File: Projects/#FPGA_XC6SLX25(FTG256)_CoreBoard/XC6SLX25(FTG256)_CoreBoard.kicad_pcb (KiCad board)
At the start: 2 copper layers, 69.6 x 30 mm, 2 parts, among them J1 MTA18ASF2G72HZ-2G3A1, U1 XC6SLX25-FTG256

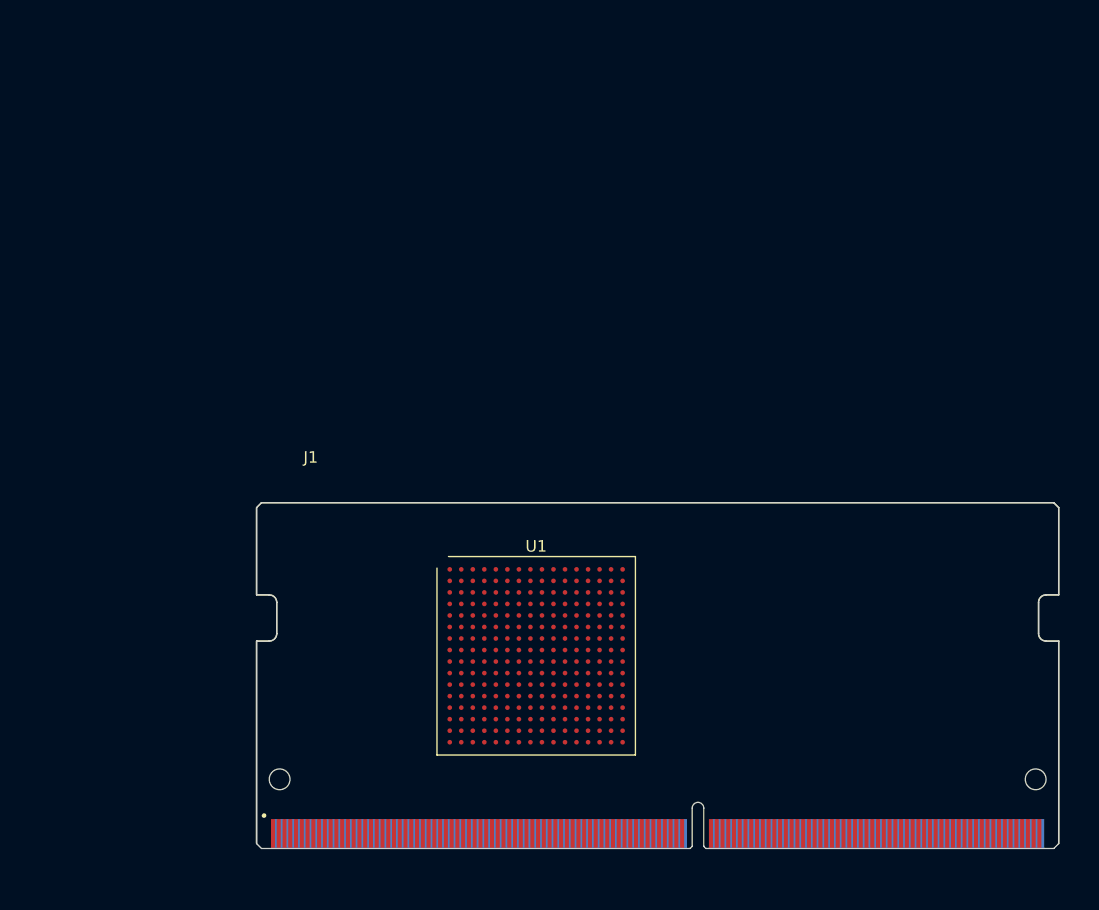
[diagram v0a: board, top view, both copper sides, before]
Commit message: Update XC6SLX25(FTG256)_CoreBoard
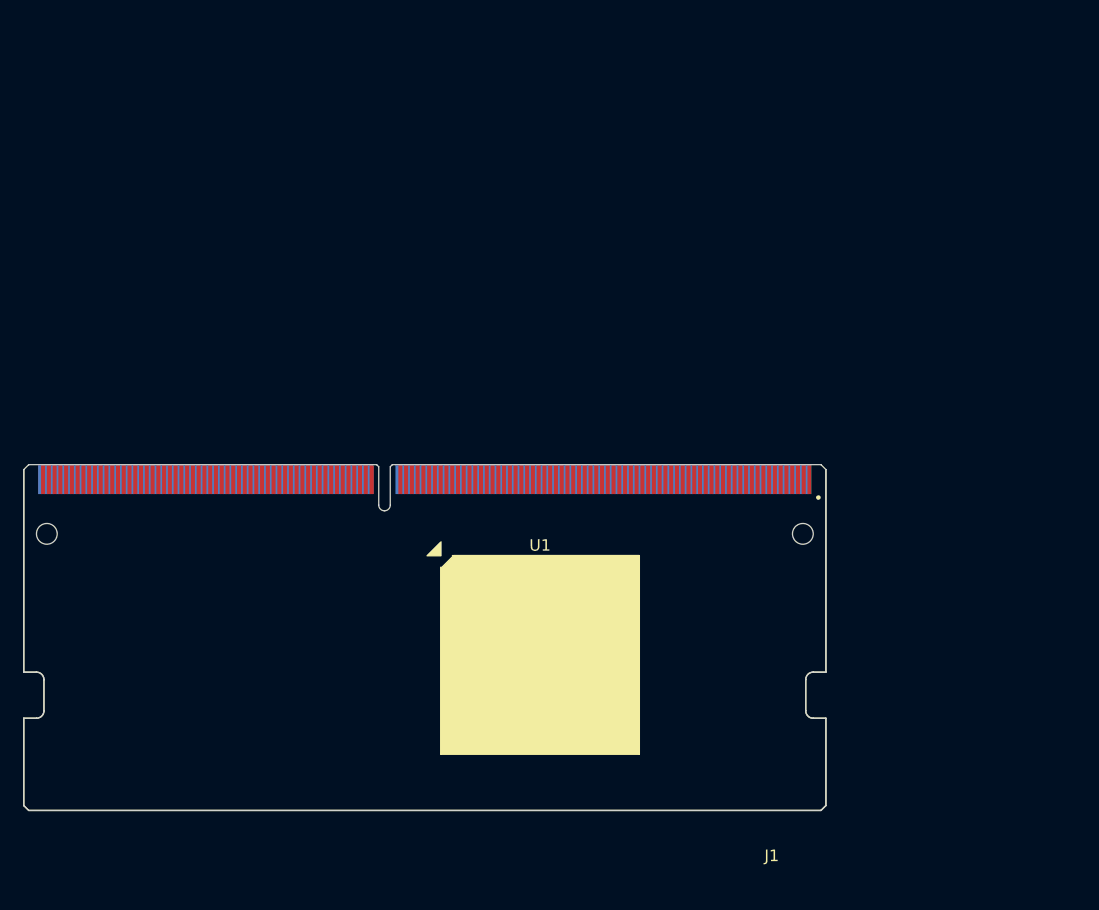
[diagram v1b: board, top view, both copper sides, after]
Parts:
- moved J1 20.5 mm to (122.0, 80.5), turned to 180 degrees
- moved U1 0.35 mm to (132.0, 82.0)
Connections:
- U1 pad A1: unconnected-(U1-PadA1) -> GND
- U1 pad A16: unconnected-(U1-PadA16) -> GND
- U1 pad B11: unconnected-(U1-PadB11) -> GND
- U1 pad B13: unconnected-(U1-PadB13) -> +3V3
- U1 pad B4: unconnected-(U1-PadB4) -> +3V3
- U1 pad B7: unconnected-(U1-PadB7) -> GND
- U1 pad B9: unconnected-(U1-PadB9) -> +3V3
- U1 pad D10: unconnected-(U1-PadD10) -> +3V3
- U1 pad D13: unconnected-(U1-PadD13) -> GND
- U1 pad D15: unconnected-(U1-PadD15) -> +2V5
- U1 pad D2: unconnected-(U1-PadD2) -> +1V5
- U1 pad D4: unconnected-(U1-PadD4) -> GND
- U1 pad D7: unconnected-(U1-PadD7) -> +3V3
- U1 pad E5: unconnected-(U1-PadE5) -> +3V3
- U1 pad E9: unconnected-(U1-PadE9) -> GND
- U1 pad F11: unconnected-(U1-PadF11) -> +3V3
- U1 pad F8: unconnected-(U1-PadF8) -> +3V3
- U1 pad G10: unconnected-(U1-PadG10) -> +3V3
- U1 pad G13: unconnected-(U1-PadG13) -> +2V5
- U1 pad G15: unconnected-(U1-PadG15) -> GND
- U1 pad G2: unconnected-(U1-PadG2) -> GND
- U1 pad G4: unconnected-(U1-PadG4) -> +1V5
- U1 pad G7: unconnected-(U1-PadG7) -> +1V2
- U1 pad G8: unconnected-(U1-PadG8) -> GND
- U1 pad G9: unconnected-(U1-PadG9) -> +1V2
- U1 pad H10: unconnected-(U1-PadH10) -> +1V2
- U1 pad H12: unconnected-(U1-PadH12) -> GND
- U1 pad H6: unconnected-(U1-PadH6) -> +3V3
- U1 pad H7: unconnected-(U1-PadH7) -> GND
- U1 pad H8: unconnected-(U1-PadH8) -> +1V2
- U1 pad H9: unconnected-(U1-PadH9) -> GND
- U1 pad J10: unconnected-(U1-PadJ10) -> +3V3
- U1 pad J15: unconnected-(U1-PadJ15) -> +2V5
- U1 pad J2: unconnected-(U1-PadJ2) -> +1V5
- U1 pad J5: unconnected-(U1-PadJ5) -> GND
- U1 pad J7: unconnected-(U1-PadJ7) -> +1V2
- U1 pad J8: unconnected-(U1-PadJ8) -> GND
- U1 pad J9: unconnected-(U1-PadJ9) -> +1V2
- U1 pad K10: unconnected-(U1-PadK10) -> +1V2
- U1 pad K13: unconnected-(U1-PadK13) -> +2V5
- U1 pad K4: unconnected-(U1-PadK4) -> +1V5
- U1 pad K7: unconnected-(U1-PadK7) -> GND
- U1 pad K8: unconnected-(U1-PadK8) -> +1V2
- U1 pad K9: unconnected-(U1-PadK9) -> GND
- U1 pad L15: unconnected-(U1-PadL15) -> GND
- U1 pad L2: unconnected-(U1-PadL2) -> GND
- U1 pad L6: unconnected-(U1-PadL6) -> +3V3
- U1 pad L9: unconnected-(U1-PadL9) -> +3V3
- U1 pad M8: unconnected-(U1-PadM8) -> GND
- U1 pad N10: unconnected-(U1-PadN10) -> +3V3
- U1 pad N13: unconnected-(U1-PadN13) -> GND
- U1 pad N15: unconnected-(U1-PadN15) -> +2V5
- U1 pad N2: unconnected-(U1-PadN2) -> +1V5
- U1 pad N7: unconnected-(U1-PadN7) -> +3V3
- U1 pad P3: unconnected-(U1-PadP3) -> GND
- U1 pad R10: unconnected-(U1-PadR10) -> GND
- U1 pad R13: unconnected-(U1-PadR13) -> +2V5
- U1 pad R4: unconnected-(U1-PadR4) -> +3V3
- U1 pad R6: unconnected-(U1-PadR6) -> GND
- U1 pad R8: unconnected-(U1-PadR8) -> +3V3
- U1 pad T1: unconnected-(U1-PadT1) -> GND
- U1 pad T16: unconnected-(U1-PadT16) -> GND
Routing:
- net GND: track 0.00 -> 17.0 mm, vias 0 -> 22
- net +3V3: track 0.00 -> 12.7 mm, vias 0 -> 17
- net +1V2: track 0.00 -> 9.90 mm, vias 0 -> 6
- net +2V5: track 0.00 -> 4.24 mm, vias 0 -> 6
- net +1V5: track 0.00 -> 3.54 mm, vias 0 -> 5
- net unconnected-(U1-PadR12): track 0.00 -> 0.71 mm, vias 0 -> 1
- net unconnected-(U1-PadP4): track 0.00 -> 0.71 mm, vias 0 -> 1
- net unconnected-(U1-PadN6): track 0.00 -> 0.71 mm, vias 0 -> 1
- net unconnected-(U1-PadN14): track 0.00 -> 0.71 mm, vias 0 -> 1
- net unconnected-(U1-PadN11): track 0.00 -> 0.71 mm, vias 0 -> 1
- net unconnected-(U1-PadM7): track 0.00 -> 0.71 mm, vias 0 -> 1
- net unconnected-(U1-PadM2): track 0.00 -> 0.71 mm, vias 0 -> 1
- net unconnected-(U1-PadL8): track 0.00 -> 0.71 mm, vias 0 -> 1
- net unconnected-(U1-PadL4): track 0.00 -> 0.71 mm, vias 0 -> 1
- net unconnected-(U1-PadL13): track 0.00 -> 0.71 mm, vias 0 -> 1
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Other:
- outline, holes or cut-outs redrawn
- copper layers 2 -> 6

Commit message: Update XC6SLX25(FTG256)_CoreBoard
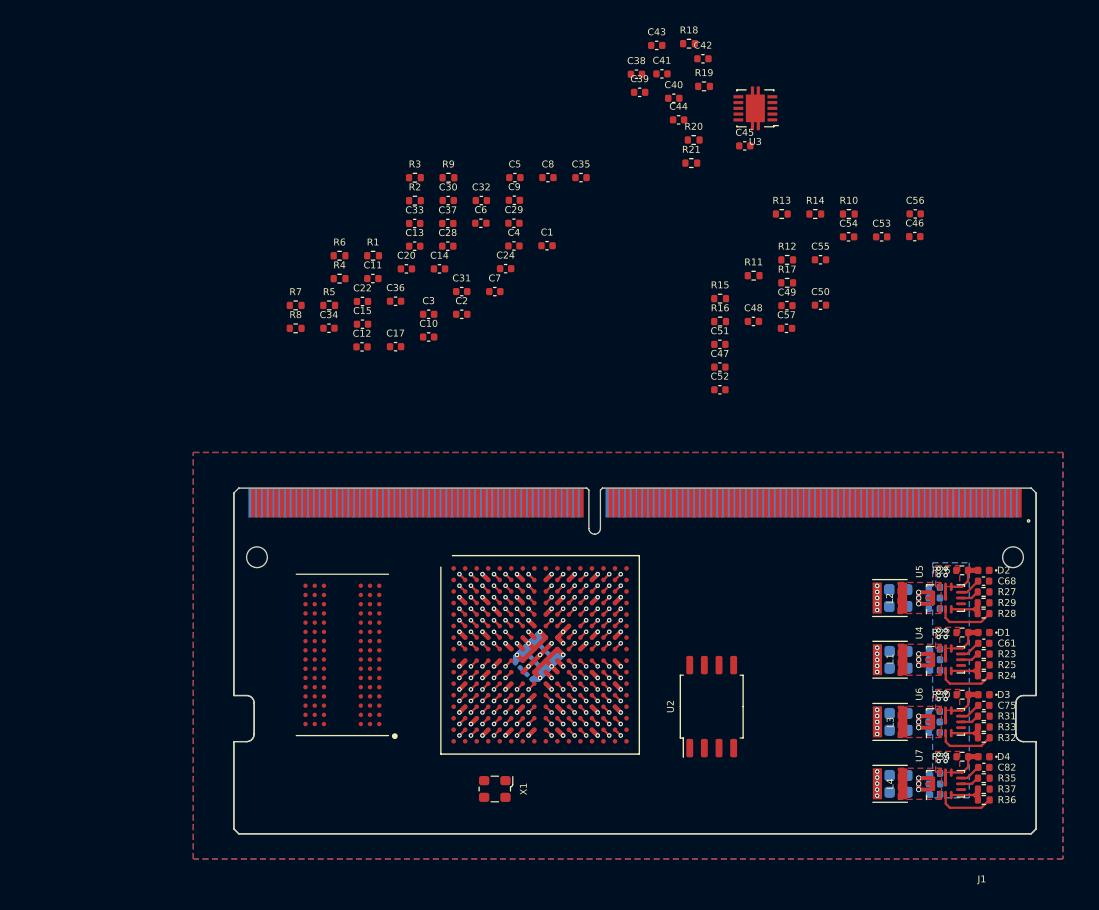
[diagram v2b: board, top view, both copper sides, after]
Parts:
- added C1: 0.1uF, Capacitor_SMD:C_0402_1005Metric, F.Cu at (132.6, 46.5)
- added C10: 10nF, Capacitor_SMD:C_0402_1005Metric, F.Cu at (122.3, 54.4)
- added C11: 0.1uF, Capacitor_SMD:C_0402_1005Metric, F.Cu at (117.5, 49.4)
- added C12: 0.1uF, Capacitor_SMD:C_0402_1005Metric, F.Cu at (116.5, 55.3)
- added C13: 10nF, Capacitor_SMD:C_0402_1005Metric, F.Cu at (121.1, 46.5)
- added C14: 0.1uF, Capacitor_SMD:C_0402_1005Metric, F.Cu at (123.3, 48.5)
- added C15: 10nF, Capacitor_SMD:C_0402_1005Metric, F.Cu at (116.6, 53.3)
- added C16: 0.1uF, Capacitor_SMD:C_0201_0603Metric, B.Cu at (131.0, 82.0)
- added C17: 0.1uF, Capacitor_SMD:C_0402_1005Metric, F.Cu at (119.5, 55.3)
- added C18: 10nF, Capacitor_SMD:C_0201_0603Metric, B.Cu at (130.1, 82.9)
- added C19: 0.1uF, Capacitor_SMD:C_0201_0603Metric, B.Cu at (132.9, 82.1)
- added C2: 10nF, Capacitor_SMD:C_0402_1005Metric, F.Cu at (125.2, 52.5)
- added C20: 10nF, Capacitor_SMD:C_0402_1005Metric, F.Cu at (120.4, 48.5)
- added C21: 10nF, Capacitor_SMD:C_0201_0603Metric, B.Cu at (131.9, 81.1)
- added C22: 0.1uF, Capacitor_SMD:C_0402_1005Metric, F.Cu at (116.6, 51.3)
- added C23: 0.1uF, Capacitor_SMD:C_0201_0603Metric, B.Cu at (132.0, 83.0)
- added C24: 10nF, Capacitor_SMD:C_0402_1005Metric, F.Cu at (129.0, 48.5)
- added C25: 10nF, Capacitor_SMD:C_0201_0603Metric, B.Cu at (131.1, 83.9)
- added C28: 0.1uF, Capacitor_SMD:C_0402_1005Metric, F.Cu at (124.0, 46.5)
- added C29: 10nF, Capacitor_SMD:C_0402_1005Metric, F.Cu at (129.7, 44.5)
- added C3: 0.1uF, Capacitor_SMD:C_0402_1005Metric, F.Cu at (122.3, 52.5)
- added C30: 0.1uF, Capacitor_SMD:C_0402_1005Metric, F.Cu at (124.0, 42.6)
- added C31: 10nF, Capacitor_SMD:C_0402_1005Metric, F.Cu at (125.2, 50.5)
- added C32: 0.1uF, Capacitor_SMD:C_0402_1005Metric, F.Cu at (126.9, 42.6)
- added C33: 10nF, Capacitor_SMD:C_0402_1005Metric, F.Cu at (121.1, 44.6)
- added C34: 0.1uF, Capacitor_SMD:C_0402_1005Metric, F.Cu at (113.7, 53.7)
- added C35: 10nF, Capacitor_SMD:C_0402_1005Metric, F.Cu at (135.6, 40.6)
- added C36: 0.1uF, Capacitor_SMD:C_0402_1005Metric, F.Cu at (119.5, 51.3)
- added C37: 10nF, Capacitor_SMD:C_0402_1005Metric, F.Cu at (124.0, 44.6)
- added C38: 10uF, Capacitor_SMD:C_0402_1005Metric, F.Cu at (140.4, 31.6)
- added C39: 10uF, Capacitor_SMD:C_0402_1005Metric, F.Cu at (140.6, 33.2)
- added C4: 0.1uF, Capacitor_SMD:C_0402_1005Metric, F.Cu at (129.7, 46.5)
- added C40: 10uF, Capacitor_SMD:C_0402_1005Metric, F.Cu at (143.6, 33.7)
- added C41: 10uF, Capacitor_SMD:C_0402_1005Metric, F.Cu at (142.6, 31.6)
- added C42: 1nF, Capacitor_SMD:C_0402_1005Metric, F.Cu at (146.1, 30.3)
- added C43: 10uF, Capacitor_SMD:C_0402_1005Metric, F.Cu at (142.1, 29.1)
- added C44: 0.1uF, Capacitor_SMD:C_0402_1005Metric, F.Cu at (144.0, 35.6)
- added C45: 4.7uF, Capacitor_SMD:C_0402_1005Metric, F.Cu at (149.8, 37.8)
- added C46: 0.1uF, Capacitor_SMD:C_0402_1005Metric, F.Cu at (164.5, 45.7)
- added C47: 0.1uF, Capacitor_SMD:C_0402_1005Metric, F.Cu at (147.6, 57.0)
- added C48: 0.1uF, Capacitor_SMD:C_0402_1005Metric, F.Cu at (150.5, 53.1)
- added C49: 0.1uF, Capacitor_SMD:C_0402_1005Metric, F.Cu at (153.4, 51.7)
- added C5: 10nF, Capacitor_SMD:C_0402_1005Metric, F.Cu at (129.8, 40.6)
- added C50: 0.1uF, Capacitor_SMD:C_0402_1005Metric, F.Cu at (156.3, 51.7)
- added C51: 0.1uF, Capacitor_SMD:C_0402_1005Metric, F.Cu at (147.6, 55.1)
- added C52: 0.1uF, Capacitor_SMD:C_0402_1005Metric, F.Cu at (147.6, 59.0)
- added C53: 0.1uF, Capacitor_SMD:C_0402_1005Metric, F.Cu at (161.6, 45.7)
- added C54: 0.1uF, Capacitor_SMD:C_0402_1005Metric, F.Cu at (158.8, 45.7)
- added C55: 0.1uF, Capacitor_SMD:C_0402_1005Metric, F.Cu at (156.3, 47.7)
- added C56: 0.1uF, Capacitor_SMD:C_0402_1005Metric, F.Cu at (164.6, 43.7)
- added C57: 0.1uF, Capacitor_SMD:C_0402_1005Metric, F.Cu at (153.4, 53.7)
- added C58: 10uF, Capacitor_SMD:C_0402_1005Metric, B.Cu at (166.2, 81.5)
- added C59: 10uF, Capacitor_SMD:C_0402_1005Metric, B.Cu at (166.2, 83.3)
- added C6: 10nF, Capacitor_SMD:C_0402_1005Metric, F.Cu at (126.9, 44.5)
- added C60: 0.1uF, Capacitor_SMD:C_0402_1005Metric, B.Cu at (166.2, 82.4)
- added C61: 1uF, Capacitor_SMD:C_0402_1005Metric, F.Cu at (170.5, 81.0)
- added C63: 22uF, Capacitor_SMD:C_0603_1608Metric, B.Cu at (163.1, 83.2)
- added C64: 22uF, Capacitor_SMD:C_0603_1608Metric, B.Cu at (163.1, 81.7)
- added C65: 10uF, Capacitor_SMD:C_0402_1005Metric, B.Cu at (166.2, 76.1)
- added C66: 10uF, Capacitor_SMD:C_0402_1005Metric, B.Cu at (166.2, 77.1)
- added C67: 0.1uF, Capacitor_SMD:C_0402_1005Metric, B.Cu at (166.2, 78.0)
- added C68: 1uF, Capacitor_SMD:C_0402_1005Metric, F.Cu at (170.5, 75.6)
- added C7: 0.1uF, Capacitor_SMD:C_0402_1005Metric, F.Cu at (128.1, 50.5)
- added C70: 22uF, Capacitor_SMD:C_0603_1608Metric, B.Cu at (163.1, 77.8)
- added C71: 22uF, Capacitor_SMD:C_0603_1608Metric, B.Cu at (163.1, 76.3)
- added C72: 10uF, Capacitor_SMD:C_0402_1005Metric, B.Cu at (166.2, 92.3)
- added C73: 10uF, Capacitor_SMD:C_0402_1005Metric, B.Cu at (166.2, 93.2)
- added C74: 0.1uF, Capacitor_SMD:C_0402_1005Metric, B.Cu at (166.2, 94.1)
- added C75: 1uF, Capacitor_SMD:C_0402_1005Metric, F.Cu at (170.5, 86.4)
- added C77: 22uF, Capacitor_SMD:C_0603_1608Metric, B.Cu at (163.1, 87.1)
- added C78: 22uF, Capacitor_SMD:C_0603_1608Metric, B.Cu at (163.1, 88.5)
- added C79: 10uF, Capacitor_SMD:C_0402_1005Metric, B.Cu at (166.2, 87.8)
- added C8: 0.1uF, Capacitor_SMD:C_0402_1005Metric, F.Cu at (132.7, 40.6)
- added C80: 10uF, Capacitor_SMD:C_0402_1005Metric, B.Cu at (166.2, 88.7)
- added C81: 0.1uF, Capacitor_SMD:C_0402_1005Metric, B.Cu at (166.2, 86.9)
- added C82: 1uF, Capacitor_SMD:C_0402_1005Metric, F.Cu at (170.5, 91.8)
- added C84: 22uF, Capacitor_SMD:C_0603_1608Metric, B.Cu at (163.1, 93.9)
- added C85: 22uF, Capacitor_SMD:C_0603_1608Metric, B.Cu at (163.1, 92.5)
- added C9: 10nF, Capacitor_SMD:C_0402_1005Metric, F.Cu at (129.8, 42.6)
- added D1: LED, LED_SMD:LED_0402_1005Metric, F.Cu at (170.5, 80.1)
- added D2: LED, LED_SMD:LED_0402_1005Metric, F.Cu at (170.5, 74.7)
- added D3: LED, LED_SMD:LED_0402_1005Metric, F.Cu at (170.5, 85.5)
- added D4: LED, LED_SMD:LED_0402_1005Metric, F.Cu at (170.5, 90.8)
- added DDR3-1: MT41J128M16JT-125, lib:DDR3-BGA96, F.Cu at (114.8, 82.0)
- added L1: 0.47uH, Inductor_SMD:L_Taiyo-Yuden_NR-30xx, F.Cu at (162.4, 82.4)
- added L2: 0.47uH, Inductor_SMD:L_Taiyo-Yuden_NR-30xx, F.Cu at (162.3, 77.1)
- added L3: 0.47uH, Inductor_SMD:L_Taiyo-Yuden_NR-30xx, F.Cu at (162.4, 87.8)
- added L4: 0.47uH, Inductor_SMD:L_Taiyo-Yuden_NR-30xx, F.Cu at (162.4, 93.2)
- added R1: 22R, Resistor_SMD:R_0402_1005Metric, F.Cu at (117.5, 47.4)
- added R10: 100R, Resistor_SMD:R_0402_1005Metric, F.Cu at (158.8, 43.8)
- added R11: 100R, Resistor_SMD:R_0402_1005Metric, F.Cu at (150.5, 49.1)
- added R12: 4K7, Resistor_SMD:R_0402_1005Metric, F.Cu at (153.4, 47.7)
- added R13: 100R, Resistor_SMD:R_0402_1005Metric, F.Cu at (153.0, 43.8)
- added R14: 100R, Resistor_SMD:R_0402_1005Metric, F.Cu at (155.9, 43.8)
- added R15: 4K7, Resistor_SMD:R_0402_1005Metric, F.Cu at (147.6, 51.1)
- added R16: 4K7, Resistor_SMD:R_0402_1005Metric, F.Cu at (147.6, 53.1)
- added R17: 240R, Resistor_SMD:R_0402_1005Metric, F.Cu at (153.4, 49.7)
- added R18: 10K, Resistor_SMD:R_0402_1005Metric, F.Cu at (144.9, 29.0)
- added R19: 10K, Resistor_SMD:R_0402_1005Metric, F.Cu at (146.2, 32.7)
- added R2: 10K, Resistor_SMD:R_0402_1005Metric, F.Cu at (121.1, 42.6)
- added R20: 100K, Resistor_SMD:R_0402_1005Metric, F.Cu at (145.3, 37.3)
- added R21: 10K, Resistor_SMD:R_0402_1005Metric, F.Cu at (145.1, 39.3)
- added R22: 5K, Resistor_SMD:R_0402_1005Metric, F.Cu at (168.6, 80.1)
- added R23: 100K, Resistor_SMD:R_0402_1005Metric, F.Cu at (170.5, 81.9)
- added R24: 200K, Resistor_SMD:R_0402_1005Metric, F.Cu at (170.5, 83.8)
- added R25: 44.2K, Resistor_SMD:R_0402_1005Metric, F.Cu at (170.5, 82.9)
- added R26: 2K, Resistor_SMD:R_0402_1005Metric, F.Cu at (168.6, 74.7)
- added R27: 100K, Resistor_SMD:R_0402_1005Metric, F.Cu at (170.5, 76.5)
- added R28: 200K, Resistor_SMD:R_0402_1005Metric, F.Cu at (170.5, 78.4)
- added R29: 63.2K, Resistor_SMD:R_0402_1005Metric, F.Cu at (170.5, 77.5)
- added R3: 10K, Resistor_SMD:R_0402_1005Metric, F.Cu at (121.1, 40.6)
- added R30: 2K, Resistor_SMD:R_0402_1005Metric, F.Cu at (168.6, 85.5)
- added R31: 100K, Resistor_SMD:R_0402_1005Metric, F.Cu at (170.5, 87.3)
- added R32: 200K, Resistor_SMD:R_0402_1005Metric, F.Cu at (170.5, 89.2)
- added R33: 200K, Resistor_SMD:R_0402_1005Metric, F.Cu at (170.5, 88.3)
- added R34: 2K, Resistor_SMD:R_0402_1005Metric, F.Cu at (168.6, 90.8)
- added R35: 100K, Resistor_SMD:R_0402_1005Metric, F.Cu at (170.5, 92.7)
- added R36: 200K, Resistor_SMD:R_0402_1005Metric, F.Cu at (170.5, 94.6)
- added R37: 133.3K, Resistor_SMD:R_0402_1005Metric, F.Cu at (170.5, 93.6)
- added R4: 22R, Resistor_SMD:R_0402_1005Metric, F.Cu at (114.6, 49.4)
- added R5: 10K, Resistor_SMD:R_0402_1005Metric, F.Cu at (113.7, 51.7)
- added R6: 10K, Resistor_SMD:R_0402_1005Metric, F.Cu at (114.6, 47.4)
- added R7: 10K, Resistor_SMD:R_0402_1005Metric, F.Cu at (110.8, 51.7)
- added R8: 0R, Resistor_SMD:R_0402_1005Metric, F.Cu at (110.8, 53.7)
- added R9: 10K, Resistor_SMD:R_0402_1005Metric, F.Cu at (124.0, 40.6)
- added U2: W25Q128JVS, Package_SO:SOIC-8_5.23x5.23mm_P1.27mm, F.Cu at (146.9, 86.5)
- added U3: TPS51200DRC, Package_SON:VSON-10-1EP_3x3mm_P0.5mm_EP1.65x2.4mm, F.Cu at (150.7, 34.6)
- added U4: MP214x, lib:MP2145, F.Cu at (167.2, 82.4)
- added U5: MP214x, lib:MP2145, F.Cu at (167.2, 77.1)
- added U6: MP214x, lib:MP2145, F.Cu at (167.2, 87.8)
- added U7: MP214x, lib:MP2145, F.Cu at (167.2, 93.2)
- added X1: ECS-2520MV-xxx-xx, Oscillator:Oscillator_SMD_ECS_2520MV-xxx-xx-4Pin_2.5x2.0mm, F.Cu at (128.1, 93.6)
- moved J1 18.3 mm to (140.2, 82.5)
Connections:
- J1 pad 1: unconnected-(J1-Pad1) -> TCK
- J1 pad 3: unconnected-(J1-Pad3) -> TMS
- J1 pad 5: unconnected-(J1-Pad5) -> TDO
- J1 pad 7: unconnected-(J1-Pad7) -> TDI
- U1 pad A15: unconnected-(U1-PadA15) -> TMS
- U1 pad A2: unconnected-(U1-PadA2) -> /DDR_A9
- U1 pad A3: unconnected-(U1-PadA3) -> /DDR_VREF
- U1 pad B1: unconnected-(U1-PadB1) -> /DDR_BA2
- U1 pad B2: unconnected-(U1-PadB2) -> /DDR_A8
- U1 pad B3: unconnected-(U1-PadB3) -> /DDR_CS1
- U1 pad C1: unconnected-(U1-PadC1) -> /DDR_WE
- U1 pad C12: unconnected-(U1-PadC12) -> TDI
- U1 pad C14: unconnected-(U1-PadC14) -> TCK
- U1 pad C2: unconnected-(U1-PadC2) -> /DDR_BA1
- U1 pad C3: unconnected-(U1-PadC3) -> /DDR_BA0
- U1 pad C4: unconnected-(U1-PadC4) -> Net-(R1-Pad1)
- U1 pad D1: unconnected-(U1-PadD1) -> /DDR_A2
- U1 pad D3: unconnected-(U1-PadD3) -> /DDR_A7
- U1 pad E1: unconnected-(U1-PadE1) -> /DDR_CLK-
- U1 pad E14: unconnected-(U1-PadE14) -> TDO
- U1 pad E2: unconnected-(U1-PadE2) -> /DDR_CLK+
- U1 pad E3: unconnected-(U1-PadE3) -> /DDR_A11
- U1 pad E4: unconnected-(U1-PadE4) -> /DDR_RESET
- U1 pad F1: unconnected-(U1-PadF1) -> /DDR_D5
- U1 pad F2: unconnected-(U1-PadF2) -> /DDR_D4
- U1 pad F3: unconnected-(U1-PadF3) -> /DDR_A12
- U1 pad F4: unconnected-(U1-PadF4) -> /DDR_CKE
- U1 pad F5: unconnected-(U1-PadF5) -> /DDR_A14
- U1 pad F6: unconnected-(U1-PadF6) -> /DDR_A13
- U1 pad G1: unconnected-(U1-PadG1) -> /DDR_D7
- U1 pad G3: unconnected-(U1-PadG3) -> /DDR_D6
- U1 pad G5: unconnected-(U1-PadG5) -> /DDR_A4
- U1 pad G6: unconnected-(U1-PadG6) -> /DDR_A10
- U1 pad H1: unconnected-(U1-PadH1) -> /DDR_LDQS-
- U1 pad H2: unconnected-(U1-PadH2) -> /DDR_LDQS+
- U1 pad H3: unconnected-(U1-PadH3) -> /DDR_A6
- U1 pad H4: unconnected-(U1-PadH4) -> /DDR_A5
- U1 pad H5: unconnected-(U1-PadH5) -> /DDR_~{CAS}
- U1 pad J1: unconnected-(U1-PadJ1) -> /DDR_D3
- U1 pad J3: unconnected-(U1-PadJ3) -> /DDR_D2
- U1 pad J4: unconnected-(U1-PadJ4) -> /DDR_LDM
- U1 pad J6: unconnected-(U1-PadJ6) -> /DDR_~{RAS}
- U1 pad K1: unconnected-(U1-PadK1) -> /DDR_D1
- U1 pad K2: unconnected-(U1-PadK2) -> /DDR_D0
- U1 pad K3: unconnected-(U1-PadK3) -> /DDR_UDM
- U1 pad K5: unconnected-(U1-PadK5) -> /DDR_A0
- U1 pad K6: unconnected-(U1-PadK6) -> /DDR_A1
- U1 pad L1: unconnected-(U1-PadL1) -> /DDR_D9
- U1 pad L11: unconnected-(U1-PadL11) -> Net-(R9-Pad1)
- U1 pad L3: unconnected-(U1-PadL3) -> /DDR_D8
- U1 pad L4: unconnected-(U1-PadL4) -> /DDR_A3
- U1 pad L5: unconnected-(U1-PadL5) -> /DDR_ODT
- U1 pad M1: unconnected-(U1-PadM1) -> /DDR_D11
- U1 pad M2: unconnected-(U1-PadM2) -> /DDR_D10
- U1 pad M3: unconnected-(U1-PadM3) -> /DDR_VREF
- U1 pad N1: unconnected-(U1-PadN1) -> /DDR_UDQS-
- U1 pad N11: unconnected-(U1-PadN11) -> Net-(R4-Pad1)
- U1 pad N12: unconnected-(U1-PadN12) -> Flash_MISO_2
- U1 pad N3: unconnected-(U1-PadN3) -> /DDR_UDQS+
- U1 pad P1: unconnected-(U1-PadP1) -> /DDR_D13
- U1 pad P10: unconnected-(U1-PadP10) -> Flash_MISO_1
- U1 pad P12: unconnected-(U1-PadP12) -> Flash_MISO_3
- U1 pad P13: unconnected-(U1-PadP13) -> Net-(R6-Pad1)
- U1 pad P14: unconnected-(U1-PadP14) -> Net-(R8-Pad1)
- U1 pad P2: unconnected-(U1-PadP2) -> /DDR_D12
- U1 pad P7: unconnected-(U1-PadP7) -> GCLK
- U1 pad R1: unconnected-(U1-PadR1) -> /DDR_D15
- U1 pad R11: unconnected-(U1-PadR11) -> Flash_CLK
- U1 pad R2: unconnected-(U1-PadR2) -> /DDR_D14
- U1 pad R3: unconnected-(U1-PadR3) -> Net-(R5-Pad1)
- U1 pad T10: unconnected-(U1-PadT10) -> Flash_MOSI
- U1 pad T11: unconnected-(U1-PadT11) -> Net-(R3-Pad1)
- U1 pad T2: unconnected-(U1-PadT2) -> Net-(R7-Pad1)
- U1 pad T3: unconnected-(U1-PadT3) -> Flash_CS
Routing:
- net +1V2: track 9.90 -> 31.4 mm, vias 6 -> 11
- net GND: track 17.0 -> 28.9 mm, vias 22 -> 34
- net +3V3: track 12.7 -> 17.7 mm, vias 17 -> 22
- net +1V5: track 3.54 -> 8.55 mm, vias 5 -> 10
- net +2V5: track 4.24 -> 9.26 mm, vias 6 -> 11
- net Net-(R32-Pad2): track 0.00 -> 3.92 mm
- net Net-(R24-Pad2): track 0.00 -> 3.92 mm
- net Net-(R36-Pad2): track 0.00 -> 3.92 mm
- net Net-(R28-Pad2): track 0.00 -> 3.92 mm
- net Net-(D3-Pad2): track 0.00 -> 3.45 mm
- net Net-(D4-Pad2): track 0.00 -> 3.45 mm
- net Net-(D1-Pad2): track 0.00 -> 3.45 mm
- net Net-(D2-Pad2): track 0.00 -> 3.45 mm
- net Net-(C82-Pad1): track 0.00 -> 1.87 mm
- net Net-(C75-Pad1): track 0.00 -> 1.87 mm
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- added copper zone on B.Cu, net 5V
- added copper zone on F.Cu, net 5V
- added copper zone on B.Cu, net GND
- added copper zone on F.Cu, net GND
- added copper zone on In1.Cu, net GND
- added copper zone on In2.Cu, net GND
- added copper zone on In3.Cu, net GND
- added copper zone on In4.Cu, net GND
- added copper zone on F.Cu, net Net-(L1-Pad1)
- added copper zone on F.Cu, net Net-(L2-Pad1)
- added copper zone on F.Cu, net Net-(L3-Pad1)
- added copper zone on F.Cu, net Net-(L4-Pad1)
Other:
- outline, holes or cut-outs redrawn

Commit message: Update XC6SLX25(FTG256)_CoreBoard
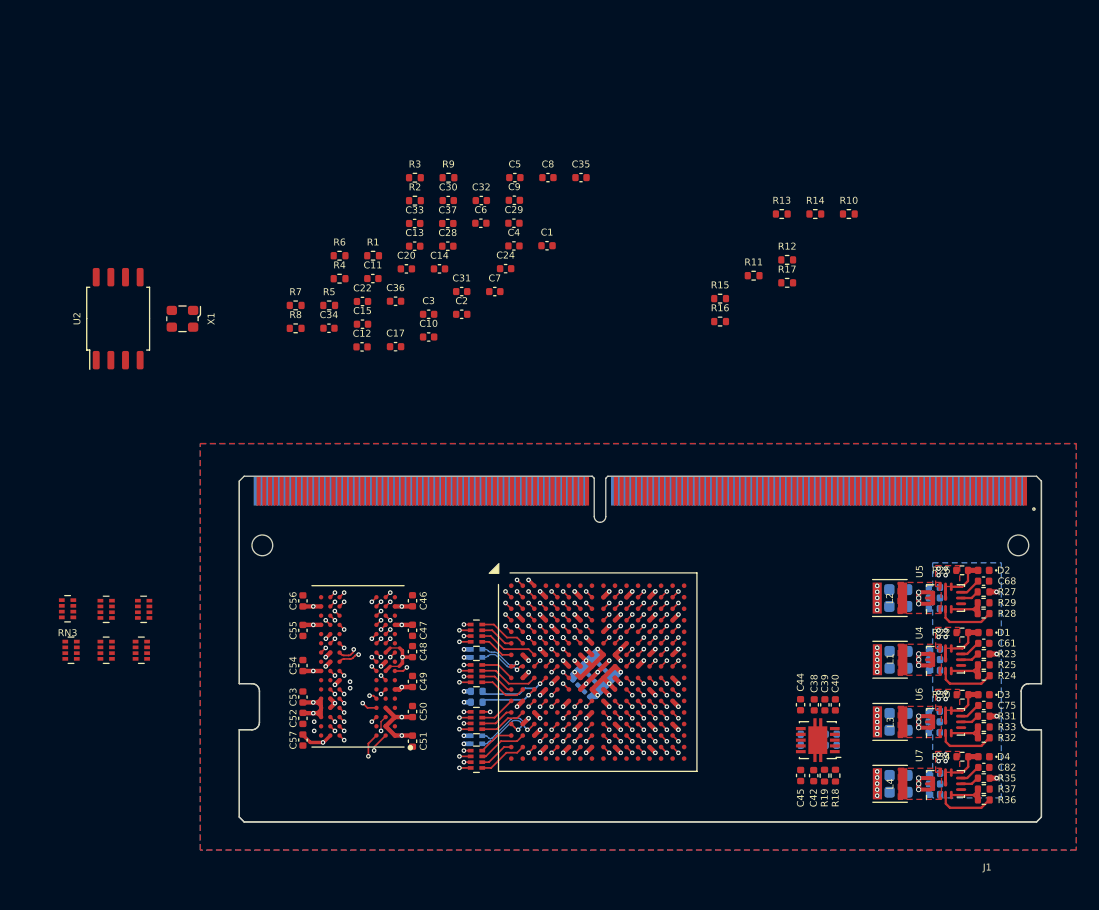
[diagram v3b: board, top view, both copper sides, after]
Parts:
- added R38: R, Resistor_SMD:R_0402_1005Metric, B.Cu at (126.5, 86.1)
- added R39: R, Resistor_SMD:R_0402_1005Metric, B.Cu at (126.5, 85.2)
- added RN1: R_Pack04, Resistor_SMD:R_Array_Concave_4x0402, F.Cu at (97.4, 81.6)
- added RN10: R_Pack04, Resistor_SMD:R_Array_Concave_4x0402, F.Cu at (126.5, 91.1)
- added RN11: R_Pack02, Resistor_SMD:R_Array_Convex_2x0402, B.Cu at (126.5, 89.4)
- added RN12: R_Pack02, Resistor_SMD:R_Array_Convex_2x0402, B.Cu at (126.5, 81.9)
- added RN2: R_Pack04, Resistor_SMD:R_Array_Concave_4x0402, F.Cu at (94.3, 81.6)
- added RN3: R_Pack04, Resistor_SMD:R_Array_Concave_4x0402, F.Cu at (91.0, 78.0)
- added RN4: R_Pack04, Resistor_SMD:R_Array_Concave_4x0402, F.Cu at (91.3, 81.6)
- added RN5: R_Pack04, Resistor_SMD:R_Array_Concave_4x0402, F.Cu at (94.3, 78.0)
- added RN6: R_Pack04, Resistor_SMD:R_Array_Concave_4x0402, F.Cu at (97.6, 78.0)
- added RN7: R_Pack04, Resistor_SMD:R_Array_Concave_4x0402, F.Cu at (126.5, 83.6)
- added RN8: R_Pack04, Resistor_SMD:R_Array_Concave_4x0402, F.Cu at (126.5, 80.1)
- added RN9: R_Pack04, Resistor_SMD:R_Array_Concave_4x0402, F.Cu at (126.5, 87.7)
- C41, C43, R20, R21: moved to B.Cu
- moved R18 64.8 mm to (157.6, 92.5), turned to 90 degrees
- moved C53 64.2 mm to (111.4, 85.7), turned to 90 degrees
- moved C42 62.9 mm to (155.7, 92.5), turned to -90 degrees
- moved C56 62.9 mm to (111.4, 77.3), turned to 90 degrees
- moved C43 61.6 mm to (157.3, 88.9), turned to 180 degrees
- moved U2 61.5 mm to (95.4, 52.8)
- moved R19 60.7 mm to (156.7, 92.5), turned to -90 degrees
- moved C54 60.2 mm to (111.4, 82.9), turned to 90 degrees
- moved C41 60.1 mm to (157.3, 89.8), turned to 180 degrees
- moved C38 56.9 mm to (155.8, 86.3), turned to 90 degrees
- moved C39 55.5 mm to (156.7, 86.3), turned to 90 degrees
- moved C55 55.2 mm to (111.4, 79.9), turned to -90 degrees
- moved C57 55.1 mm to (111.4, 89.4), turned to -90 degrees
- moved U3 55.1 mm to (156.1, 89.4)
- moved C45 54.8 mm to (154.6, 92.5), turned to -90 degrees
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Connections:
- U1 pad F1: /DDR_D5 -> /DDR_MD5
- U1 pad F2: /DDR_D4 -> /DDR_MD4
- U1 pad G1: /DDR_D7 -> /DDR_MD7
- U1 pad G3: /DDR_D6 -> /DDR_MD6
- U1 pad H1: /DDR_LDQS- -> /DDR_MLDQS-
- U1 pad H2: /DDR_LDQS+ -> /DDR_MLDQS+
- U1 pad J1: /DDR_D3 -> /DDR_MD3
- U1 pad J3: /DDR_D2 -> /DDR_MD2
- U1 pad J4: /DDR_LDM -> /DDR_MLDM
- U1 pad K1: /DDR_D1 -> /DDR_MD1
- U1 pad K2: /DDR_D0 -> /DDR_MD0
- U1 pad K3: /DDR_UDM -> /DDR_MUDM
- U1 pad L1: /DDR_D9 -> /DDR_MD9
- U1 pad L3: /DDR_D8 -> /DDR_MD8
- U1 pad M1: /DDR_D11 -> /DDR_MD11
- U1 pad M2: /DDR_D10 -> /DDR_MD10
- U1 pad N1: /DDR_UDQS- -> /DDR_MUDQS-
- U1 pad N3: /DDR_UDQS+ -> /DDR_MUDQS+
- U1 pad P1: /DDR_D13 -> /DDR_MD13
- U1 pad P2: /DDR_D12 -> /DDR_MD12
- U1 pad R1: /DDR_D15 -> /DDR_MD15
- U1 pad R2: /DDR_D14 -> /DDR_MD14
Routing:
- net +1V5: track 8.55 -> 39.6 mm, vias 10 -> 24
- net /DDR_D3: track 0.00 -> 14.0 mm, vias 0 -> 2
- net /DDR_D14: track 0.71 -> 14.2 mm, vias 1 -> 2
- net /DDR_D1: track 0.00 -> 13.1 mm, vias 0 -> 2
- net /DDR_UDQS-: track 0.00 -> 12.4 mm, vias 0 -> 2
- net /DDR_LDM: track 0.71 -> 12.9 mm, vias 1 -> 2
- net /DDR_D10: track 0.71 -> 12.9 mm, vias 1 -> 2
- net /DDR_UDQS+: track 0.71 -> 12.4 mm, vias 1 -> 2
- net /DDR_D12: track 0.71 -> 12.3 mm, vias 1 -> 2
- net /DDR_D8: track 0.71 -> 11.8 mm, vias 1 -> 2
- net /DDR_D15: track 0.00 -> 11.0 mm, vias 0 -> 2
- net /DDR_D13: track 0.00 -> 10.1 mm, vias 0 -> 2
- net /DDR_UDM: track 0.71 -> 10.8 mm, vias 1 -> 2
- net /DDR_D0: track 0.71 -> 10.6 mm, vias 1 -> 2
- net /DDR_D9: track 0.00 -> 9.21 mm, vias 0 -> 2
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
